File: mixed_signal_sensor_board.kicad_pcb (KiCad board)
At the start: 4 copper layers, 128 x 77.5 mm, 154 parts, among them J1 Conn_01x02, J10 Conn_01x04, J11 Conn_01x04, J12 USB_C_Receptacle_USB2.0_16P, J13 Conn_01x04, J14 PYRO, J15 PYRO, J16 PYRO, J17 PYRO, J2 Conn_01x04, J3 Conn_01x06, J4 Conn_01x04, J5 Conn_01x04, J6 Conn_01x04, J7 Conn_01x04, J8 Conn_01x04, J9 Conn_01x04, Q1 Q_NMOS_GDS, Q2 Q_NMOS_GDS, Q3 Q_NMOS_GDS, Q4 Q_NMOS_GDS, SW1 SW_Push, SW2 SW_Push, U1 TMP117xxDRV, U2 LM27762, U3 MagI3C_171013201, U4 TPS7A20xxxDBV, U5 TPS7A20xxxDBV, U6 ADS131M08xPBS, U7 STM32L552CEUx, U8 TCAN3414DRBR, Y1 SG-8018CE_8.192M-TJHSA

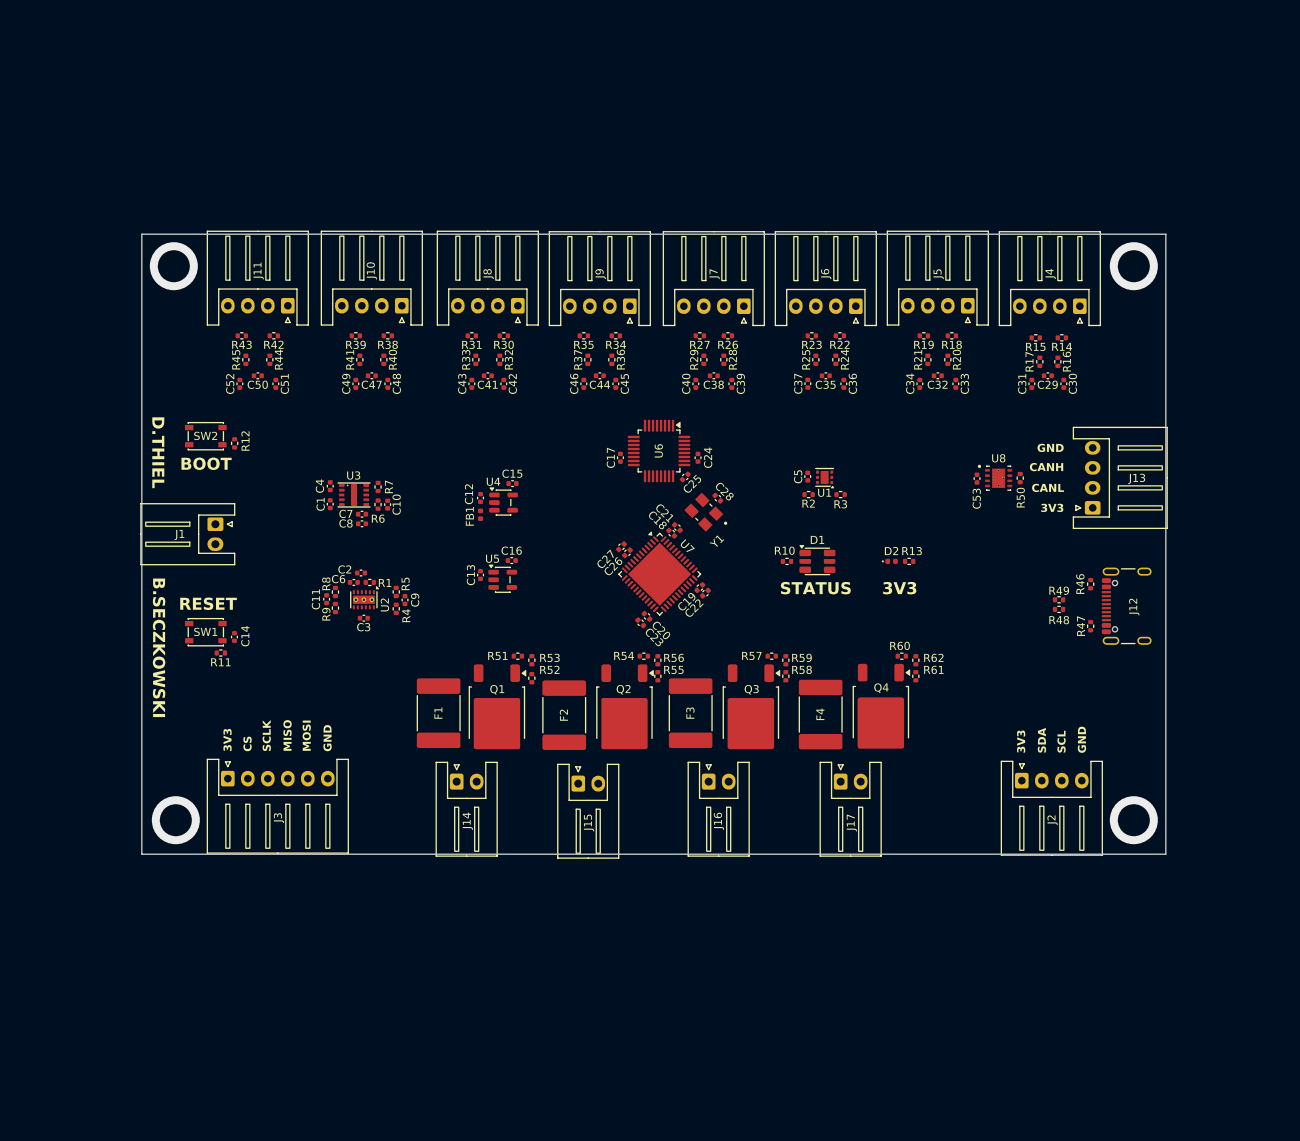
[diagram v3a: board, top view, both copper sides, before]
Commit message: Step files, SMD connectors, reduced size
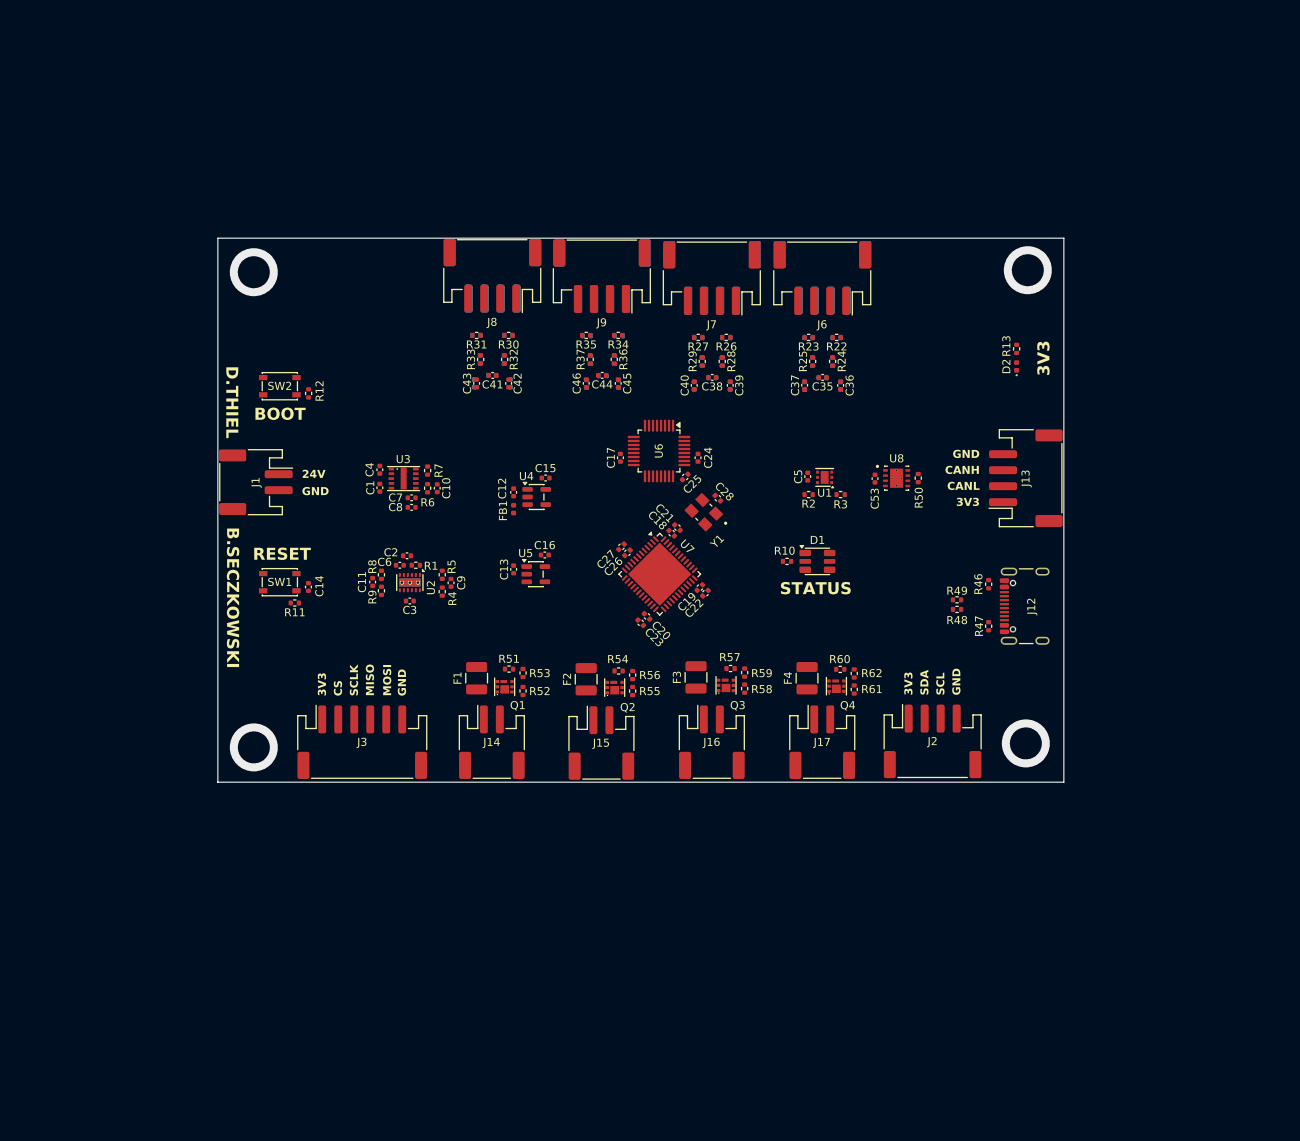
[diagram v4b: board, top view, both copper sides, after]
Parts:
- C29, C30, C31, C32, C33, C34, C47, C48, C49, C50, C51, C52, R14, R15, R16, R17, R18, R19, R20, R21, R38, R39, R40, R41, R42, R43, R44, R45: moved to B.Cu
- F1, F2, F3, F4: footprint Fuse:Fuse_2920_7451Metric -> Fuse:Fuse_1210_3225Metric
- J1, J14, J15, J16, J17: footprint Connector_JST:JST_XH_S2B-XH-A_1x02_P2.50mm_Horizontal -> Connector_JST:JST_PH_S2B-PH-SM4-TB_1x02-1MP_P2.00mm_Horizontal
- J10, J11, J4, J5: footprint Connector_JST:JST_XH_S4B-XH-A_1x04_P2.50mm_Horizontal -> Connector_JST:JST_PH_S4B-PH-SM4-TB_1x04-1MP_P2.00mm_Horizontal; moved to B.Cu
- J13, J2, J6, J7, J8, J9: footprint Connector_JST:JST_XH_S4B-XH-A_1x04_P2.50mm_Horizontal -> Connector_JST:JST_PH_S4B-PH-SM4-TB_1x04-1MP_P2.00mm_Horizontal
- J3: footprint Connector_JST:JST_XH_S6B-XH-A_1x06_P2.50mm_Horizontal -> Connector_JST:JST_PH_S6B-PH-SM4-TB_1x06-1MP_P2.00mm_Horizontal
- Q1, Q2, Q3, Q4: value Q_NMOS_GDS -> CSD17571Q2; footprint Package_TO_SOT_SMD:TO-252-2 -> ElecSuper_ESN7414:ElecSuper_ESN7414
- moved J4 32.3 mm to (177.8, 57.0), turned to 0 degrees
- moved J5 32.1 mm to (164.1, 57.0), turned to 0 degrees
- moved R13 29.8 mm to (202.1, 65.8), turned to -90 degrees
- moved C50 29.3 mm to (136.6, 69.2), turned to 0 degrees
- moved C51 29.3 mm to (138.8, 70.2)
- moved C52 29.3 mm to (134.3, 70.2)
- moved R42 29.3 mm to (138.6, 64.2), turned to 0 degrees
- moved R43 29.3 mm to (134.6, 64.2), turned to 0 degrees
- moved R44 29.3 mm to (138.1, 67.2)
- moved R45 29.3 mm to (135.1, 67.2)
- moved D2 29.0 mm to (202.1, 68.0), turned to 90 degrees
- moved C47 28.8 mm to (150.3, 69.2), turned to 0 degrees
- moved C48 28.8 mm to (152.3, 70.2)
- moved C49 28.8 mm to (148.3, 70.2)
- moved R38 28.8 mm to (152.3, 64.2), turned to 0 degrees
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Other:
- board size 128 x 77.5 mm -> 105.8 x 68 mm
- board text added: "24V"

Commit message: Delvin protection, USB ESD protection, 02x06 pin socket
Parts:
- added D3: D_Zener, Diode_SMD:D_0402_1005Metric, F.Cu at (118.3, 84.4)
- added J18: Conn_02x06_Odd_Even, Connector_PinSocket_2.54mm:PinSocket_2x06_P2.54mm_Vertical_SMD, F.Cu at (194.4, 66.0)
- added Q5: Q_PMOS, Package_TO_SOT_SMD:SOT-23, F.Cu at (119.1, 81.2)
- added R63: 100K, Resistor_SMD:R_0402_1005Metric, F.Cu at (121.2, 84.4)
- added U9: TCAN3414DRBR, TCAN3414DRBR:XCVR_TCAN3414DRBR, F.Cu at (187.1, 82.0)
- Q1, Q2, Q3, Q4: footprint ElecSuper_ESN7414:ElecSuper_ESN7414 -> CSD17571Q2:CSD17571Q2
- U8: value TCAN3414DRBR -> USBLC6-2P6; footprint TCAN3414DRBR:XCVR_TCAN3414DRBR -> Package_TO_SOT_SMD:SOT-666
- moved U8 16.5 mm to (192.0, 97.8), turned to 180 degrees
- moved D2 13.6 mm to (195.6, 56.1), turned to 180 degrees
- moved R13 13.1 mm to (193.4, 56.1), turned to 0 degrees
- moved C1 3.60 mm to (126.1, 83.2)
- moved C10 3.60 mm to (133.3, 83.3)
- moved C4 3.60 mm to (126.1, 81.0)
- moved C7 3.60 mm to (130.1, 84.5)
- moved C8 3.60 mm to (130.1, 85.7)
- moved R6 3.60 mm to (132.1, 83.3)
- moved R7 3.60 mm to (132.1, 81.1)
- moved U3 3.60 mm to (129.1, 82.1)
- moved FB1 1.71 mm to (138.7, 84.2), turned to 180 degrees
- moved C12 1.15 mm to (139.1, 82.6)
- moved C15 1.15 mm to (143.1, 80.8)
- moved U4 1.15 mm to (142.0, 83.2)
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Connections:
- J1 pad 1: +24V -> Net-(D3-K)
- R48 pad 2: /USB_N -> Net-(R48-Pad2)
- R49 pad 2: /USB_P -> Net-(R49-Pad2)
- U7 pad 12: unconnected-(U7-PA2-Pad12) -> /PA2
- U7 pad 13: unconnected-(U7-PA3-Pad13) -> /PA3
- U7 pad 2: unconnected-(U7-PC13-Pad2) -> /PC13
- U7 pad 25: unconnected-(U7-PB12-Pad25) -> /PB12
- U7 pad 26: unconnected-(U7-PB13-Pad26) -> /PB13
- U7 pad 27: unconnected-(U7-PB14-Pad27) -> /PB14
- U7 pad 3: unconnected-(U7-PC14-Pad3) -> /PC14
- U7 pad 4: unconnected-(U7-PC15-Pad4) -> /PC15
- U8 pad 1: /CAN_TX -> Net-(R48-Pad2)
- U8 pad 3: +3V3 -> Net-(R49-Pad2)
- U8 pad 4: /CAN_RX -> /USB_P
- U8 pad 5: GND -> unconnected-(U8-VBUS-Pad5)
- U8 pad 6: /CAN/CAN_L -> /USB_N
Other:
- board text added: "PA2"
- board text added: "PA3"
- board text added: "PB12"
- board text added: "PB13"
- board text added: "PB14"
- board text added: "PC13"
- board text added: "PC14"
- board text added: "PC15"
- board text added: "PYRO1"
- board text added: "PYRO2"
- board text added: "PYRO3"
- board text added: "PYRO4"
- board text added: "SB1"
- board text added: "SB2"
- board text added: "SB3"
- board text added: "SB4"
- board text added: "SB5"
- board text added: "SB6"
- board text added: "SB7"
- board text added: "SB8"

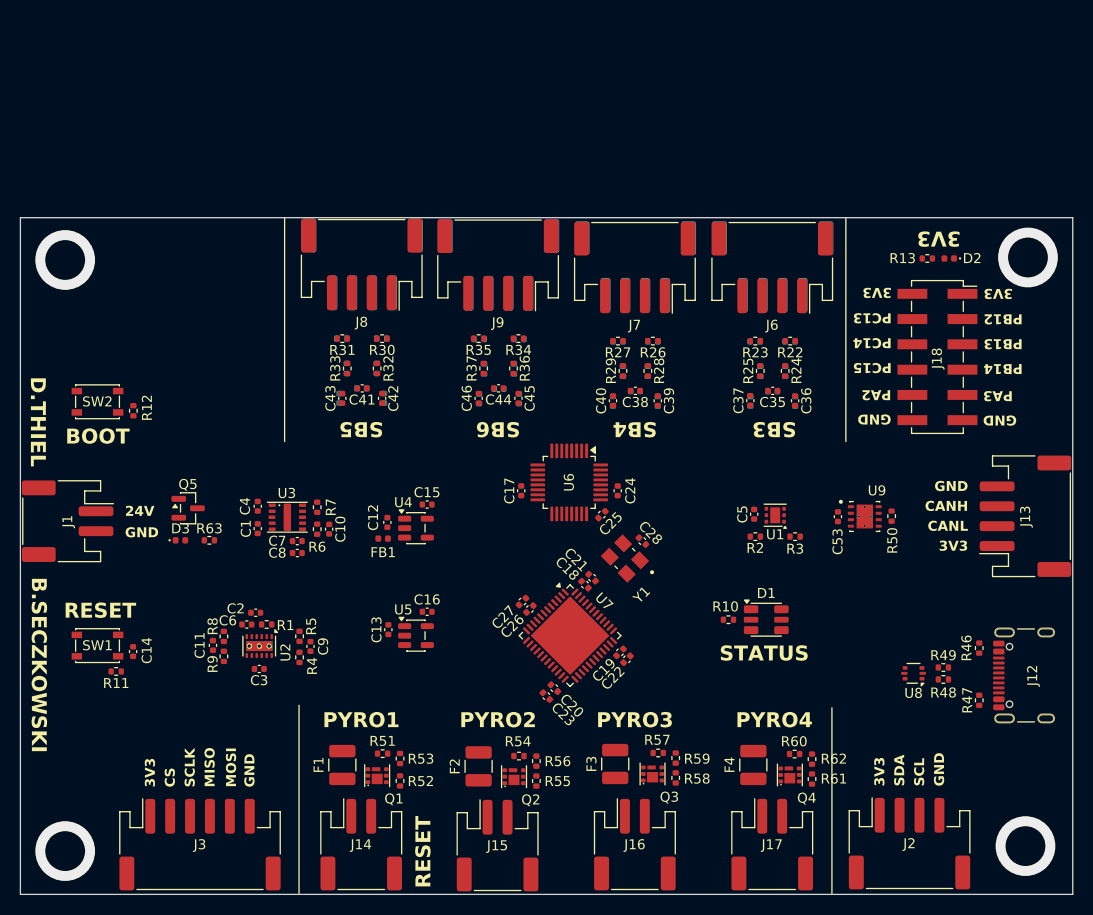
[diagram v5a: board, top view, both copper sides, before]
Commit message: replaced signal blocks, shortening board, adding precise positioning
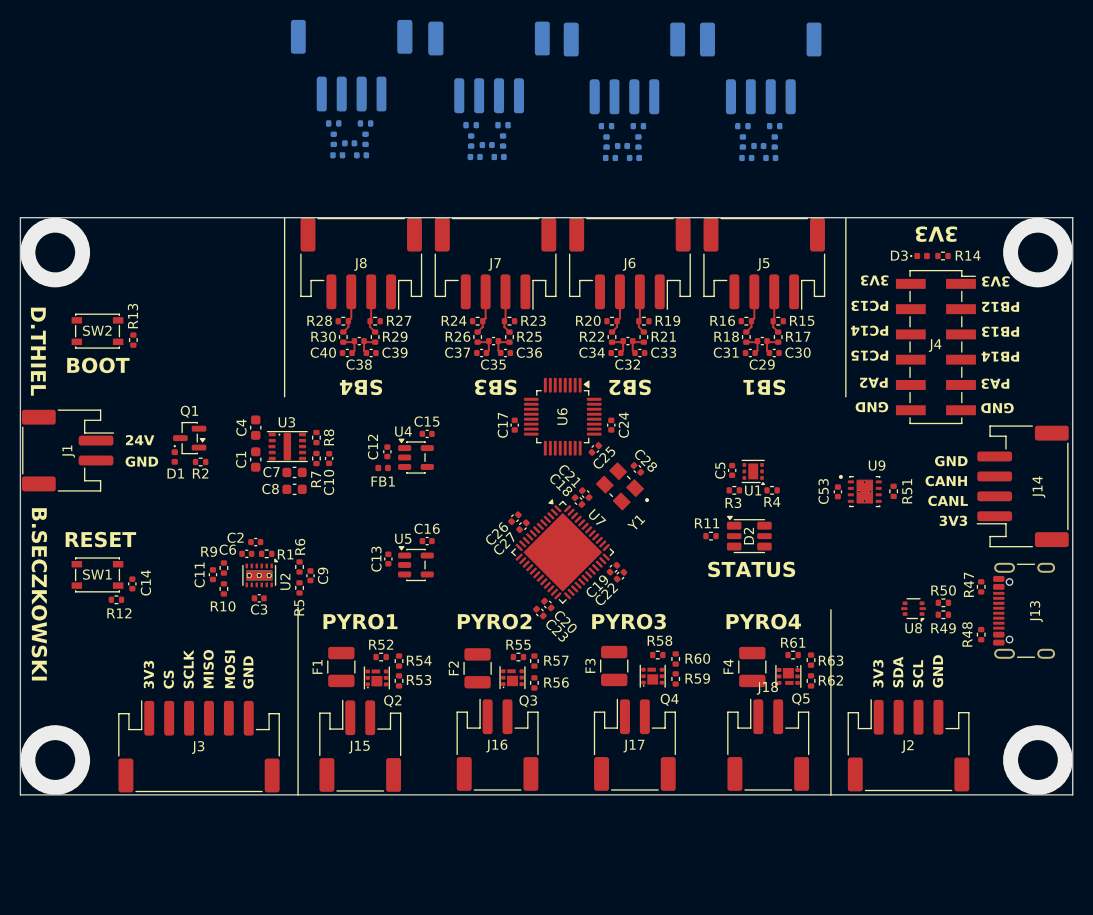
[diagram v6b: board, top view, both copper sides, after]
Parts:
- C1, C4, C7, C8: footprint Capacitor_SMD:C_0402_1005Metric -> Capacitor_SMD:C_0603_1608Metric
- C29, C30, C31, C32, C33, C34, J5, R15, R17, R19, R21: moved to F.Cu
- C41, C42, C43, C44, C45, C46, J9, R31, R33, R35, R37: moved to B.Cu
- D1: value SMLVN6RGB -> 30V; footprint LED_SMD:LED_ROHM_SMLVN6 -> Diode_SMD:D_0402_1005Metric
- D2: value LED -> SMLVN6RGB; footprint LED_SMD:LED_0402_1005Metric -> LED_SMD:LED_ROHM_SMLVN6
- D3: value D_Zener -> LED; footprint Diode_SMD:D_0402_1005Metric -> LED_SMD:LED_0402_1005Metric
- J12: value USB_C_Receptacle_USB2.0_16P -> Conn_01x04; footprint Connector_USB:USB_C_Receptacle_GCT_USB4105-xx-A_16P_TopMnt_Horizontal -> Connector_JST:JST_PH_S4B-PH-SM4-TB_1x04-1MP_P2.00mm_Horizontal; moved to B.Cu
- J13: value Conn_01x04 -> USB_C_Receptacle_USB2.0_16P; footprint Connector_JST:JST_PH_S4B-PH-SM4-TB_1x04-1MP_P2.00mm_Horizontal -> Connector_USB:USB_C_Receptacle_GCT_USB4105-xx-A_16P_TopMnt_Horizontal
- J14: value PYRO -> Conn_01x04; footprint Connector_JST:JST_PH_S2B-PH-SM4-TB_1x02-1MP_P2.00mm_Horizontal -> Connector_JST:JST_PH_S4B-PH-SM4-TB_1x04-1MP_P2.00mm_Horizontal
- J18: value Conn_02x06_Odd_Even -> PYRO; footprint Connector_PinSocket_2.54mm:PinSocket_2x06_P2.54mm_Vertical_SMD -> Connector_JST:JST_PH_S2B-PH-SM4-TB_1x02-1MP_P2.00mm_Horizontal
- J4: value Conn_01x04 -> Conn_02x06_Odd_Even; footprint Connector_JST:JST_PH_S4B-PH-SM4-TB_1x04-1MP_P2.00mm_Horizontal -> Connector_PinSocket_2.54mm:PinSocket_2x06_P2.54mm_Vertical_SMD; moved to F.Cu
- Q1: value CSD17571Q2 -> IRLML5103TRPBF; footprint CSD17571Q2:CSD17571Q2 -> Package_TO_SOT_SMD:SOT-23
- Q5: value Q_PMOS -> CSD17571Q2; footprint Package_TO_SOT_SMD:SOT-23 -> CSD17571Q2:CSD17571Q2
- R10: value 120R -> 10K
- R11: value 4K7 -> 120R
- R13: value 120R -> 4K7
- R14: value 1MΩ -> 120R; moved to F.Cu
- R16, R20: value 10K -> 1MΩ; moved to F.Cu
- R18: value 1MΩ -> 10K; moved to F.Cu
- R2: value 5K -> 100K
- R22, R26, R30, R38, R42: value 1MΩ -> 10K
- R24, R28, R40, R44: value 10K -> 1MΩ
- R32, R36: value 10K -> 1MΩ; moved to B.Cu
- R34: value 1MΩ -> 10K; moved to B.Cu
- R4: value 10K -> 5K
- R46: value 5K1 -> 10K; moved to B.Cu
- R48: value 22R -> 5K1
- R50: value 120R -> 22R
- R51: value 10K -> 120R
- R52, R55, R58, R61: value 70K -> 10K
- R53, R56, R59, R62: value 10K -> 70K
- R6, R63: value 100K -> 10K
- R7: value 16K9 -> 100K
- R8: value 10K -> 16K9
- moved R13 80.2 mm to (113.6, 64.3), turned to 90 degrees
- moved D3 79.8 mm to (192.9, 55.9)
- moved J14 75.6 mm to (203.0, 79.0), turned to 90 degrees
- moved J12 67.0 mm to (176.7, 37.0), turned to 0 degrees
- moved Q5 62.6 mm to (179.4, 98.1), turned to -90 degrees
- moved R63 61.6 mm to (181.7, 96.5), turned to 90 degrees
- moved D1 61.6 mm to (117.8, 76.0), turned to -90 degrees
- moved R11 61.3 mm to (171.7, 84.0)
- moved R51 57.7 mm to (190.0, 79.5), turned to 90 degrees
- moved R2 56.2 mm to (120.4, 76.5), turned to 0 degrees
- moved R46 56.1 mm to (174.8, 44.4)
- moved R10 50.8 mm to (122.7, 89.3), turned to -90 degrees
- moved R4 50.4 mm to (177.8, 79.4), turned to 0 degrees
- moved R45 48.6 mm to (178.1, 44.4), turned to -90 degrees
- moved R43 48.5 mm to (178.1, 42.8)
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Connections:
- D1 pad 1: /LEDB -> Net-(D1-K)
- D1 pad 2: Net-(D1-RA) -> Net-(D1-A)
- D2 pad 1: GND -> /LEDB
- D2 pad 2: Net-(D2-A) -> Net-(D2-RA)
- D3 pad 1: Net-(D3-K) -> GND
- F1 pad 2: Net-(J14-Pin_1) -> Net-(J15-Pin_1)
- F2 pad 2: Net-(J15-Pin_1) -> Net-(J16-Pin_1)
- F3 pad 2: Net-(J16-Pin_1) -> Net-(J17-Pin_1)
- F4 pad 2: Net-(J17-Pin_1) -> Net-(J18-Pin_1)
- J1 pad 1: Net-(D3-K) -> Net-(D1-K)
- J10 pad 2: /SB7/SIGNAL_P -> /SB6/SIGNAL_P
- J10 pad 3: /SB7/SIGNAL_N -> /SB6/SIGNAL_N
- J11 pad 2: /SB8/SIGNAL_P -> /SB7/SIGNAL_P
- J11 pad 3: /SB8/SIGNAL_N -> /SB7/SIGNAL_N
- J14 pad 1: Net-(J14-Pin_1) -> +3V3
- J14 pad 2: Net-(J14-Pin_2) -> /CAN/CAN_L
- J18 pad 1: +3V3 -> Net-(J18-Pin_1)
- J18 pad 2: +3V3 -> Net-(J18-Pin_2)
- J4 pad 1: +5V -> +3V3
- J4 pad 2: /SB1/SIGNAL_P -> +3V3
- J4 pad 3: /SB1/SIGNAL_N -> /PB12
- J4 pad 4: -5V -> /PC13
- J5 pad 2: /SB2/SIGNAL_P -> /SB1/SIGNAL_P
- J5 pad 3: /SB2/SIGNAL_N -> /SB1/SIGNAL_N
- J6 pad 2: /SB3/SIGNAL_P -> /SB2/SIGNAL_P
- J6 pad 3: /SB3/SIGNAL_N -> /SB2/SIGNAL_N
- J7 pad 2: /SB4/SIGNAL_P -> /SB3/SIGNAL_P
- J7 pad 3: /SB4/SIGNAL_N -> /SB3/SIGNAL_N
- J8 pad 2: /SB5/SIGNAL_P -> /SB4/SIGNAL_P
- J8 pad 3: /SB5/SIGNAL_N -> /SB4/SIGNAL_N
- J9 pad 2: /SB6/SIGNAL_P -> /SB5/SIGNAL_P
- J9 pad 3: /SB6/SIGNAL_N -> /SB5/SIGNAL_N
- Q2 pad G: /PYRO2_SIGNAL -> /PYRO1_SIGNAL
- Q3 pad G: /PYRO3_SIGNAL -> /PYRO2_SIGNAL
- Q4 pad G: /PYRO4_SIGNAL -> /PYRO3_SIGNAL
- R10 pad 1: /LEDR -> /FB-
- R10 pad 2: Net-(D1-RA) -> GND
- R11 pad 1: +3V3 -> /LEDR
- R11 pad 2: /NRST -> Net-(D2-RA)
- R12 pad 1: /BOOT0 -> +3V3
- R12 pad 2: GND -> /NRST
- R13 pad 1: +3V3 -> /BOOT0
- R13 pad 2: Net-(D2-A) -> GND
- R14 pad 1: +3V3A -> +3V3
- R14 pad 2: /SB1/SIGNAL_P -> Net-(D3-A)
- R15 pad 1: /SB1/SIGNAL_N -> +3V3A
- R15 pad 2: GND -> /SB1/SIGNAL_P
- R16 pad 1: /SB1/SIGNAL_P -> /SB1/SIGNAL_N
- R16 pad 2: /SB1/AOUT_P -> GND
- R17 pad 1: /SB1/SIGNAL_N -> /SB1/SIGNAL_P
- R17 pad 2: /SB1/AOUT_N -> /SB1/AOUT_P
- R18 pad 1: +3V3A -> /SB1/SIGNAL_N
- R18 pad 2: /SB2/SIGNAL_P -> /SB1/AOUT_N
- R19 pad 1: /SB2/SIGNAL_N -> +3V3A
- R19 pad 2: GND -> /SB2/SIGNAL_P
- R2 pad 1: /SDA -> Net-(D1-A)
- R2 pad 2: +3V3 -> GND
- R20 pad 1: /SB2/SIGNAL_P -> /SB2/SIGNAL_N
- R20 pad 2: /SB2/AOUT_P -> GND
- R21 pad 1: /SB2/SIGNAL_N -> /SB2/SIGNAL_P
- R21 pad 2: /SB2/AOUT_N -> /SB2/AOUT_P
- R22 pad 1: +3V3A -> /SB2/SIGNAL_N
- R22 pad 2: /SB3/SIGNAL_P -> /SB2/AOUT_N
- R23 pad 1: /SB3/SIGNAL_N -> +3V3A
- R23 pad 2: GND -> /SB3/SIGNAL_P
- R24 pad 1: /SB3/SIGNAL_P -> /SB3/SIGNAL_N
- R24 pad 2: /SB3/AOUT_P -> GND
- R25 pad 1: /SB3/SIGNAL_N -> /SB3/SIGNAL_P
- R25 pad 2: /SB3/AOUT_N -> /SB3/AOUT_P
- R26 pad 1: +3V3A -> /SB3/SIGNAL_N
- R26 pad 2: /SB4/SIGNAL_P -> /SB3/AOUT_N
- R27 pad 1: /SB4/SIGNAL_N -> +3V3A
- R27 pad 2: GND -> /SB4/SIGNAL_P
- R28 pad 1: /SB4/SIGNAL_P -> /SB4/SIGNAL_N
- R28 pad 2: /SB4/AOUT_P -> GND
- R29 pad 1: /SB4/SIGNAL_N -> /SB4/SIGNAL_P
- R29 pad 2: /SB4/AOUT_N -> /SB4/AOUT_P
- R3 pad 1: /SCL -> /SDA
- R30 pad 1: +3V3A -> /SB4/SIGNAL_N
- R30 pad 2: /SB5/SIGNAL_P -> /SB4/AOUT_N
- R31 pad 1: /SB5/SIGNAL_N -> +3V3A
- R31 pad 2: GND -> /SB5/SIGNAL_P
- R32 pad 1: /SB5/SIGNAL_P -> /SB5/SIGNAL_N
- R32 pad 2: /SB5/AOUT_P -> GND
- R33 pad 1: /SB5/SIGNAL_N -> /SB5/SIGNAL_P
- R33 pad 2: /SB5/AOUT_N -> /SB5/AOUT_P
- R34 pad 1: +3V3A -> /SB5/SIGNAL_N
- R34 pad 2: /SB6/SIGNAL_P -> /SB5/AOUT_N
- R35 pad 1: /SB6/SIGNAL_N -> +3V3A
- R35 pad 2: GND -> /SB6/SIGNAL_P
- R36 pad 1: /SB6/SIGNAL_P -> /SB6/SIGNAL_N
- R36 pad 2: /SB6/AOUT_P -> GND
- R37 pad 1: /SB6/SIGNAL_N -> /SB6/SIGNAL_P
- R37 pad 2: /SB6/AOUT_N -> /SB6/AOUT_P
- R38 pad 1: +3V3A -> /SB6/SIGNAL_N
- R38 pad 2: /SB7/SIGNAL_P -> /SB6/AOUT_N
- R39 pad 1: /SB7/SIGNAL_N -> +3V3A
- R39 pad 2: GND -> /SB7/SIGNAL_P
- R4 pad 1: +5V -> /SCL
- R4 pad 2: /FB+ -> +3V3
- R40 pad 1: /SB7/SIGNAL_P -> /SB7/SIGNAL_N
- R40 pad 2: /SB7/AOUT_P -> GND
- R41 pad 1: /SB7/SIGNAL_N -> /SB7/SIGNAL_P
- R41 pad 2: /SB7/AOUT_N -> /SB7/AOUT_P
- R42 pad 1: +3V3A -> /SB7/SIGNAL_N
- R42 pad 2: /SB8/SIGNAL_P -> /SB7/AOUT_N
- R43 pad 1: /SB8/SIGNAL_N -> +3V3A
- R43 pad 2: GND -> /SB8/SIGNAL_P
- R44 pad 1: /SB8/SIGNAL_P -> /SB8/SIGNAL_N
- R44 pad 2: /SB8/AOUT_P -> GND
- R45 pad 1: /SB8/SIGNAL_N -> /SB8/SIGNAL_P
- R45 pad 2: /SB8/AOUT_N -> /SB8/AOUT_P
- R46 pad 1: GND -> /SB8/SIGNAL_N
- R46 pad 2: Net-(J12-CC2) -> /SB8/AOUT_N
- R47 pad 2: Net-(J12-CC1) -> Net-(J13-CC2)
- R48 pad 1: /USB/DN -> GND
- R48 pad 2: Net-(R48-Pad2) -> Net-(J13-CC1)
- R49 pad 1: /USB/DP -> /USB/DN
- R5 pad 1: /FB+ -> +5V
- R5 pad 2: GND -> /FB+
- R50 pad 1: /CAN/CAN_L -> /USB/DP
- R50 pad 2: /CAN/CAN_H -> Net-(R50-Pad2)
- R51 pad 1: GND -> /CAN/CAN_L
- R51 pad 2: /PYRO1_SIGNAL -> /CAN/CAN_H
- R52 pad 1: /PYRO1_FAULT -> GND
- R52 pad 2: Net-(J14-Pin_2) -> /PYRO1_SIGNAL
- R53 pad 2: GND -> Net-(J15-Pin_2)
- R54 pad 1: GND -> /PYRO1_FAULT
- R54 pad 2: /PYRO2_SIGNAL -> GND
- R55 pad 1: /PYRO2_FAULT -> GND
- R55 pad 2: Net-(J15-Pin_2) -> /PYRO2_SIGNAL
- R56 pad 2: GND -> Net-(J16-Pin_2)
- R57 pad 1: GND -> /PYRO2_FAULT
- R57 pad 2: /PYRO3_SIGNAL -> GND
- R58 pad 1: /PYRO3_FAULT -> GND
- R58 pad 2: Net-(J16-Pin_2) -> /PYRO3_SIGNAL
- R59 pad 2: GND -> Net-(J17-Pin_2)
- R6 pad 1: +5V5 -> /FB+
- R6 pad 2: /FB -> GND
- R60 pad 1: GND -> /PYRO3_FAULT
- R60 pad 2: /PYRO4_SIGNAL -> GND
- R61 pad 1: /PYRO4_FAULT -> GND
- R61 pad 2: Net-(J17-Pin_2) -> /PYRO4_SIGNAL
- R62 pad 2: GND -> Net-(J18-Pin_2)
- R63 pad 1: Net-(D3-A) -> /PYRO4_FAULT
- R7 pad 1: /FB -> +5V5
- R7 pad 2: GND -> /FB
- R8 pad 1: -5V -> /FB
- R8 pad 2: /FB- -> GND
- R9 pad 1: /FB- -> -5V
- R9 pad 2: GND -> /FB-
- U6 pad 1: /SB3/AOUT_P -> /SB1/AOUT_P
- U6 pad 10: /SB7/AOUT_N -> /SB6/AOUT_N
- U6 pad 11: /SB8/AOUT_N -> /SB5/AOUT_N
- U6 pad 12: /SB8/AOUT_P -> /SB5/AOUT_P
- U6 pad 2: /SB3/AOUT_N -> /SB1/AOUT_N
- U6 pad 29: /SB1/AOUT_P -> /SB8/AOUT_P
- U6 pad 3: /SB4/AOUT_N -> /SB2/AOUT_N
- U6 pad 30: /SB1/AOUT_N -> /SB8/AOUT_N
- U6 pad 31: /SB2/AOUT_N -> /SB7/AOUT_N
- U6 pad 32: /SB2/AOUT_P -> /SB7/AOUT_P
- U6 pad 4: /SB4/AOUT_P -> /SB2/AOUT_P
- U6 pad 5: /SB5/AOUT_P -> /SB3/AOUT_P
- U6 pad 6: /SB5/AOUT_N -> /SB3/AOUT_N
- U6 pad 7: /SB6/AOUT_N -> /SB4/AOUT_N
- U6 pad 8: /SB6/AOUT_P -> /SB4/AOUT_P
- U6 pad 9: /SB7/AOUT_P -> /SB6/AOUT_P
- U8 pad 1: Net-(R48-Pad2) -> Net-(R49-Pad2)
- U8 pad 3: Net-(R49-Pad2) -> Net-(R50-Pad2)
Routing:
- net /SB4/SIGNAL_N: track 0.00 -> 4.37 mm
- net /SB3/SIGNAL_N: track 0.00 -> 4.37 mm
- net /SB2/SIGNAL_N: track 0.00 -> 4.37 mm
- net /SB1/SIGNAL_N: track 0.00 -> 4.37 mm
- net /SB3/SIGNAL_P: track 0.00 -> 4.30 mm
- net /SB1/SIGNAL_P: track 0.00 -> 4.30 mm
- net /SB4/SIGNAL_P: track 0.00 -> 4.30 mm
- net /SB2/SIGNAL_P: track 0.00 -> 4.30 mm
- net /SB4/AOUT_P: track 0.00 -> 2.46 mm
- net /SB3/AOUT_P: track 0.00 -> 2.46 mm
- net /SB2/AOUT_P: track 0.00 -> 2.46 mm
- net /SB1/AOUT_P: track 0.00 -> 2.46 mm
- net /SB4/AOUT_N: track 0.00 -> 2.46 mm
- net /SB3/AOUT_N: track 0.00 -> 2.46 mm
- net /SB2/AOUT_N: track 0.00 -> 2.46 mm
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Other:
- board size 105.8 x 68 mm -> 105.8 x 58 mm
- board text removed: "SB5"
- board text removed: "SB6"
